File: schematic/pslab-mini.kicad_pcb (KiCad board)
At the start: 2 copper layers, 0 parts

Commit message: Adding PCB Floorplan
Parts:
- added C1: 22uF, Capacitor_SMD:C_0805_2012Metric, F.Cu at (233.7, 71.1)
- added C10: 100nF, Capacitor_SMD:C_0603_1608Metric, F.Cu at (189.8, 50.0)
- added C11: 10uF, Capacitor_SMD:C_0805_2012Metric, F.Cu at (238.2, 74.1)
- added C12: 22uF, Capacitor_SMD:C_0805_2012Metric, F.Cu at (238.2, 77.1)
- added C13: 22uF, Capacitor_SMD:C_0805_2012Metric, F.Cu at (238.2, 80.2)
- added C14: 5.6pF, Capacitor_SMD:C_0603_1608Metric, F.Cu at (189.8, 52.5)
- added C15: 100nF, Capacitor_SMD:C_0603_1608Metric, F.Cu at (189.8, 55.0)
- added C16: 5.6pF, Capacitor_SMD:C_0603_1608Metric, F.Cu at (189.8, 57.5)
- added C17: 100nF, Capacitor_SMD:C_0603_1608Metric, F.Cu at (189.8, 60.0)
- added C18: 1uF, Capacitor_SMD:C_0603_1608Metric, F.Cu at (189.8, 62.5)
- added C19: 100nF, Capacitor_SMD:C_0603_1608Metric, F.Cu at (189.8, 65.0)
- added C2: 22uF, Capacitor_SMD:C_0805_2012Metric, F.Cu at (233.7, 74.1)
- added C20: 10pF, Capacitor_SMD:C_0603_1608Metric, F.Cu at (189.8, 67.5)
- added C21: 100nF, Capacitor_SMD:C_0603_1608Metric, F.Cu at (189.8, 70.1)
- added C22: 10uF, Capacitor_SMD:C_0805_2012Metric, F.Cu at (238.2, 83.2)
- added C23: 100nF, Capacitor_SMD:C_0603_1608Metric, F.Cu at (189.8, 72.6)
- added C24: 10pF, Capacitor_SMD:C_0603_1608Metric, F.Cu at (193.8, 45.0)
- added C25: 100nF, Capacitor_SMD:C_0603_1608Metric, F.Cu at (193.8, 47.5)
- added C26: 2.2uF, Capacitor_SMD:C_0805_2012Metric, F.Cu at (238.2, 86.2)
- added C27: 22uF, Capacitor_SMD:C_0805_2012Metric, F.Cu at (242.6, 71.1)
- added C28: 4.7uF, Capacitor_SMD:C_0805_2012Metric, F.Cu at (242.6, 74.1)
- added C29: 2.2uF, Capacitor_SMD:C_0805_2012Metric, F.Cu at (242.6, 77.1)
- added C3: 2.2uF, Capacitor_SMD:C_0805_2012Metric, F.Cu at (233.7, 77.1)
- added C30: 100nF, Capacitor_SMD:C_0603_1608Metric, F.Cu at (193.8, 50.0)
- added C31: 1uF, Capacitor_SMD:C_0603_1608Metric, F.Cu at (193.8, 52.5)
- added C32: 100nF, Capacitor_SMD:C_0603_1608Metric, F.Cu at (193.8, 55.0)
- added C33: 10nF, Capacitor_SMD:C_0603_1608Metric, F.Cu at (193.8, 57.5)
- added C34: 1uF, Capacitor_SMD:C_0603_1608Metric, F.Cu at (193.8, 60.0)
- added C35: 10pF, Capacitor_SMD:C_0603_1608Metric, F.Cu at (193.8, 62.5)
- added C36: 10pF, Capacitor_SMD:C_0603_1608Metric, F.Cu at (193.8, 65.0)
- added C37: 10uF, Capacitor_SMD:C_0805_2012Metric, F.Cu at (242.6, 80.2)
- added C38: 1uF, Capacitor_SMD:C_0603_1608Metric, F.Cu at (193.8, 67.5)
- added C39: 0.1uF, Capacitor_SMD:C_0603_1608Metric, F.Cu at (193.8, 70.1)
- added C4: 1uF, Capacitor_SMD:C_0603_1608Metric, F.Cu at (189.8, 45.0)
- added C40: 0.1uF, Capacitor_SMD:C_0603_1608Metric, F.Cu at (193.8, 72.6)
- added C41: 1uF, Capacitor_SMD:C_0603_1608Metric, F.Cu at (197.9, 45.0)
- added C42: 10uF, Capacitor_SMD:C_0805_2012Metric, F.Cu at (242.6, 83.2)
- added C43: 1uF, Capacitor_SMD:C_0603_1608Metric, F.Cu at (197.9, 47.5)
- added C44: 1.2pF, Capacitor_SMD:C_0603_1608Metric, F.Cu at (197.9, 50.0)
- added C45: 1.2pF, Capacitor_SMD:C_0603_1608Metric, F.Cu at (197.9, 52.5)
- added C5: 22uF, Capacitor_SMD:C_0805_2012Metric, F.Cu at (233.7, 80.2)
- added C6: 12pF, Capacitor_SMD:C_0603_1608Metric, F.Cu at (189.8, 47.5)
- added C7: 10uF, Capacitor_SMD:C_0805_2012Metric, F.Cu at (233.7, 83.2)
- added C8: 22uF, Capacitor_SMD:C_0805_2012Metric, F.Cu at (233.7, 86.2)
- added C9: 22uF, Capacitor_SMD:C_0805_2012Metric, F.Cu at (238.2, 71.1)
- added D1: K1N5817HW-7-F, Diode_SMD:D_SOD-123, F.Cu at (182.6, 94.1)
- added D10: White, LED_SMD:LED_0603_1608Metric, F.Cu at (150.7, 105.7)
- added D11: GREEN, LED_SMD:LED_0805_2012Metric, F.Cu at (124.8, 70.8)
- added D12: BLUE, LED_SMD:LED_0805_2012Metric, F.Cu at (160.2, 106.0)
- added D2: 1N4148W, Diode_SMD:D_SOD-123, F.Cu at (182.6, 97.5)
- added D3: 6.8V, Diode_SMD:D_SOD-123, F.Cu at (182.6, 100.8)
- added D4: 6.8V, Diode_SMD:D_SOD-123, F.Cu at (182.6, 104.2)
- added D5: 1N4148W, Diode_SMD:D_SOD-123, F.Cu at (182.6, 107.5)
- added D6: WS2812B, LED_SMD:LED_WS2812B_PLCC4_5.0x5.0mm_P3.2mm, F.Cu at (198.8, 105.8)
- added D7: White, LED_SMD:LED_0603_1608Metric, F.Cu at (150.7, 97.9)
- added D8: White, LED_SMD:LED_0603_1608Metric, F.Cu at (150.7, 100.5)
- added D9: White, LED_SMD:LED_0603_1608Metric, F.Cu at (150.7, 103.1)
- added F1: 1A, Fuse:Fuse_1206_3216Metric, F.Cu at (152.2, 94.2)
- added FID1: Fiducial, Fiducial:Fiducial_0.5mm_Mask1.5mm, F.Cu at (87.5, 55.2)
- added FID2: Fiducial, Fiducial:Fiducial_0.5mm_Mask1.5mm, F.Cu at (81.2, 101.0)
- added FID3: Fiducial, Fiducial:Fiducial_0.5mm_Mask1.5mm, F.Cu at (153.5, 107.5)
- added FLASH1: W25Q32JV, Package_SO:SOIC-8_5.3x5.3mm_P1.27mm, F.Cu at (93.0, 78.8)
- added J1: USB_C_Receptacle_USB2.0_16P, Connector_USB:USB_C_Receptacle_G-Switch_GT-USB-7010ASV, F.Cu at (160.9, 99.0)
- added J2: Battery_Cell, pslab-mini:2.0mm_connector_edge, F.Cu at (90.8, 99.6)
- added J3: Conn_Coaxial, pslab-mini:BNC_connector_dosinconn DOSIN-801-0050, F.Cu at (157.0, 81.2)
- added J4: Conn_Coaxial, pslab-mini:BNC_connector_dosinconn DOSIN-801-0050, F.Cu at (157.0, 62.2)
- added J6: Conn_01x16_Socket, Connector_PinSocket_2.54mm:PinSocket_1x16_P2.54mm_Vertical, F.Cu at (97.5, 106.0)
- added J7: Conn_02x03_Top_Bottom, TerminalBlock_WAGO:TerminalBlock_WAGO_233-503_2x03_P2.54mm, F.Cu at (83.9, 88.2)
- added J8: Conn_02x17_Odd_Even, Connector_PinSocket_2.54mm:PinSocket_2x17_P2.54mm_Vertical, F.Cu at (91.5, 55.5)
- added L1: 3.3uH, Inductor_SMD:L_0603_1608Metric, F.Cu at (197.9, 55.0)
- added L2: 3.3uH, Inductor_SMD:L_0603_1608Metric, F.Cu at (197.9, 57.5)
- added L3: 4.7uH, Inductor_SMD:L_0805_2012Metric, F.Cu at (210.6, 110.6)
- added L4: 3.3uH, Inductor_SMD:L_0603_1608Metric, F.Cu at (197.9, 60.0)
- added L5: 2.4nH, Inductor_SMD:L_0402_1005Metric, F.Cu at (243.4, 66.7)
- added MH1: MountingHole_Pad, pslab-mini:MountingHole_2.75mm_Pad, F.Cu at (82.8, 56.8)
- added MH2: MountingHole_Pad, pslab-mini:MountingHole_2.75mm_Pad, F.Cu at (140.8, 56.8)
- added MH3: MountingHole_Pad, pslab-mini:MountingHole_2.75mm_Pad, F.Cu at (140.8, 105.8)
- added MH4: MountingHole_Pad, pslab-mini:MountingHole_2.75mm_Pad, F.Cu at (82.8, 105.8)
- added NT1: NetTie_2, NetTie:NetTie-2_SMD_Pad0.5mm, F.Cu at (243.1, 88.4)
- added NT2: NetTie_2, NetTie:NetTie-2_SMD_Pad0.5mm, F.Cu at (243.1, 89.9)
- added NT3: NetTie_2, NetTie:NetTie-2_SMD_Pad0.5mm, F.Cu at (243.1, 91.4)
- added NT4: NetTie_2, NetTie:NetTie-2_SMD_Pad0.5mm, F.Cu at (243.1, 92.9)
- added NT5: NetTie_2, NetTie:NetTie-2_SMD_Pad0.5mm, F.Cu at (243.1, 94.4)
- added PCB_ANT1: ANT, Diode_SMD:D_1206_3216Metric, F.Cu at (83.2, 72.5)
- added Q1: MMBT3904, Package_TO_SOT_SMD:SOT-23, F.Cu at (218.0, 102.2)
- added Q2: MMBT3906, Package_TO_SOT_SMD:SOT-23, F.Cu at (218.0, 106.8)
- added R1: 200k, Resistor_SMD:R_0603_1608Metric, F.Cu at (197.9, 62.5)
- added R10: 1k, Resistor_SMD:R_0603_1608Metric, F.Cu at (201.9, 55.0)
- added R11: 1k, Resistor_SMD:R_0603_1608Metric, F.Cu at (201.9, 57.5)
- added R12: 200, Resistor_SMD:R_0603_1608Metric, F.Cu at (201.9, 60.0)
- added R13: 200, Resistor_SMD:R_0603_1608Metric, F.Cu at (201.9, 62.5)
- added R14: 200, Resistor_SMD:R_0603_1608Metric, F.Cu at (201.9, 65.0)
- added R16: 5k1, Resistor_SMD:R_0603_1608Metric, F.Cu at (201.9, 70.1)
- added R17: 10k, Resistor_SMD:R_0603_1608Metric, F.Cu at (201.9, 72.6)
- added R18: 200, Resistor_SMD:R_0603_1608Metric, F.Cu at (205.9, 45.0)
- added R19: 200, Resistor_SMD:R_0603_1608Metric, F.Cu at (205.9, 47.5)
- added R2: 200k, Resistor_SMD:R_0603_1608Metric, F.Cu at (197.9, 65.0)
- added R20: 5k1, Resistor_SMD:R_0603_1608Metric, F.Cu at (205.9, 50.0)
- added R21: 5k1, Resistor_SMD:R_0603_1608Metric, F.Cu at (205.9, 52.5)
- added R22: 200, Resistor_SMD:R_0603_1608Metric, F.Cu at (205.9, 55.0)
- added R23: 200, Resistor_SMD:R_0603_1608Metric, F.Cu at (205.9, 57.5)
- added R24: 5k1, Resistor_SMD:R_0603_1608Metric, F.Cu at (205.9, 60.0)
- added R25: 5k1, Resistor_SMD:R_0603_1608Metric, F.Cu at (205.9, 62.5)
- added R26: 10k, Resistor_SMD:R_0603_1608Metric, F.Cu at (205.9, 65.0)
- added R27: 10k, Resistor_SMD:R_0603_1608Metric, F.Cu at (205.9, 67.5)
- added R28: 10k, Resistor_SMD:R_0603_1608Metric, F.Cu at (205.9, 70.1)
- added R29: 10k, Resistor_SMD:R_0603_1608Metric, F.Cu at (205.9, 72.6)
- added R3: 51k, Resistor_SMD:R_0603_1608Metric, F.Cu at (197.9, 67.5)
- added R30: 10k, Resistor_SMD:R_0603_1608Metric, F.Cu at (209.9, 45.0)
- added R31: 200k, Resistor_SMD:R_0603_1608Metric, F.Cu at (209.9, 47.5)
- added R32: 10k, Resistor_SMD:R_0603_1608Metric, F.Cu at (209.9, 50.0)
- added R33: 1M, Resistor_SMD:R_0603_1608Metric, F.Cu at (209.9, 52.5)
- added R34: 200k, Resistor_SMD:R_0603_1608Metric, F.Cu at (209.9, 55.0)
- added R35: 1M, Resistor_SMD:R_0603_1608Metric, F.Cu at (209.9, 57.5)
- added R36: 0, Resistor_SMD:R_0603_1608Metric, F.Cu at (209.9, 60.0)
- added R37: 10k, Resistor_SMD:R_0603_1608Metric, F.Cu at (209.9, 62.5)
- added R38: 0, Resistor_SMD:R_0603_1608Metric, F.Cu at (209.9, 65.0)
- added R39: 0, Resistor_SMD:R_0603_1608Metric, F.Cu at (209.9, 67.5)
- added R4: 5k1, Resistor_SMD:R_0603_1608Metric, F.Cu at (197.9, 70.1)
- added R40: 0, Resistor_SMD:R_0603_1608Metric, F.Cu at (209.9, 70.1)
- added R5: 5k1, Resistor_SMD:R_0603_1608Metric, F.Cu at (197.9, 72.6)
- added R6: 100k, Resistor_SMD:R_0603_1608Metric, F.Cu at (201.9, 45.0)
- added R7: 10k, Resistor_SMD:R_0603_1608Metric, F.Cu at (201.9, 47.5)
- added R8: 180k, Resistor_SMD:R_0603_1608Metric, F.Cu at (201.9, 50.0)
- added R9: 30k, Resistor_SMD:R_0603_1608Metric, F.Cu at (201.9, 52.5)
- added SW1: Power, Button_Switch_SMD:SW_Tactile_SPST_NO_Straight_CK_PTS636Sx25SMTRLFS, F.Cu at (193.8, 81.3)
- added SW2: Reset, Button_Switch_SMD:SW_Tactile_SPST_NO_Straight_CK_PTS636Sx25SMTRLFS, F.Cu at (193.8, 88.3)
- added TP1: TestPoint, pslab-mini:Test_Point_0.8mm, F.Cu at (245.2, 47.7)
- added TP2: TestPoint, pslab-mini:Test_Point_0.8mm, F.Cu at (245.2, 49.9)
- added TP3: TestPoint, pslab-mini:Test_Point_0.8mm, F.Cu at (245.2, 52.1)
- added TP4: TestPoint, pslab-mini:Test_Point_0.8mm, F.Cu at (245.2, 54.3)
- added TP5: TestPoint, pslab-mini:Test_Point_0.8mm, F.Cu at (245.2, 56.5)
- added TP6: D+, TestPoint:TestPoint_Pad_1.0x1.0mm, F.Cu at (205.3, 91.0)
- added TP7: D-, TestPoint:TestPoint_Pad_1.0x1.0mm, F.Cu at (205.2, 77.8)
- added TP8: VINBUS, TestPoint:TestPoint_Pad_1.0x1.0mm, F.Cu at (205.2, 82.0)
- added TP9: GND, TestPoint:TestPoint_Pad_1.0x1.0mm, F.Cu at (205.2, 86.5)
- added U1: MT1470, Package_TO_SOT_SMD:SOT-23-6, F.Cu at (213.1, 85.0)
- added U10: TL082, Package_SO:SOIC-8_3.9x4.9mm_P1.27mm, F.Cu at (227.3, 92.7)
- added U11: ESP32-C3, Package_DFN_QFN:QFN-32-1EP_5x5mm_P0.5mm_EP3.7x3.7mm, F.Cu at (92.8, 70.2)
- added U2: AP3015A, Package_TO_SOT_SMD:SOT-23-5, F.Cu at (212.6, 92.2)
- added U3: IP5189T, Package_DFN_QFN:QFN-24-1EP_4x4mm_P0.5mm_EP2.6x2.6mm, F.Cu at (145.8, 97.2)
- added U4: SP0503BAHT, Package_TO_SOT_SMD:SOT-143, F.Cu at (244.1, 63.5)
- added U5: AMS1117-3.3, Package_TO_SOT_SMD:SOT-223-3_TabPin2, F.Cu at (237.0, 65.2)
- added U6: STM32H563RIT6, Package_QFP:LQFP-64_10x10mm_P0.5mm, F.Cu at (112.5, 88.0)
- added U7: TL082, Package_SO:SOIC-8_3.9x4.9mm_P1.27mm, F.Cu at (227.3, 73.0)
- added U8: MCP6S21, Package_SO:SOIC-8_3.9x4.9mm_P1.27mm, F.Cu at (227.3, 79.6)
- added U9: MCP6S21, Package_SO:SOIC-8_3.9x4.9mm_P1.27mm, F.Cu at (227.3, 86.1)
- added X1: 32kHz768, Crystal:Crystal_SMD_3215-2Pin_3.2x1.5mm, F.Cu at (115.8, 72.5)
- added Y1: Crystal_25MHz, Crystal:Crystal_SMD_5032-4Pin_5.0x3.2mm, F.Cu at (110.0, 74.2)
- added Y2: Crystal_40Mhz, Crystal:Crystal_SMD_3225-4Pin_3.2x2.5mm, F.Cu at (99.5, 70.0)
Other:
- board outline added: 85 x 56 mm
- copper layers 2 -> 4

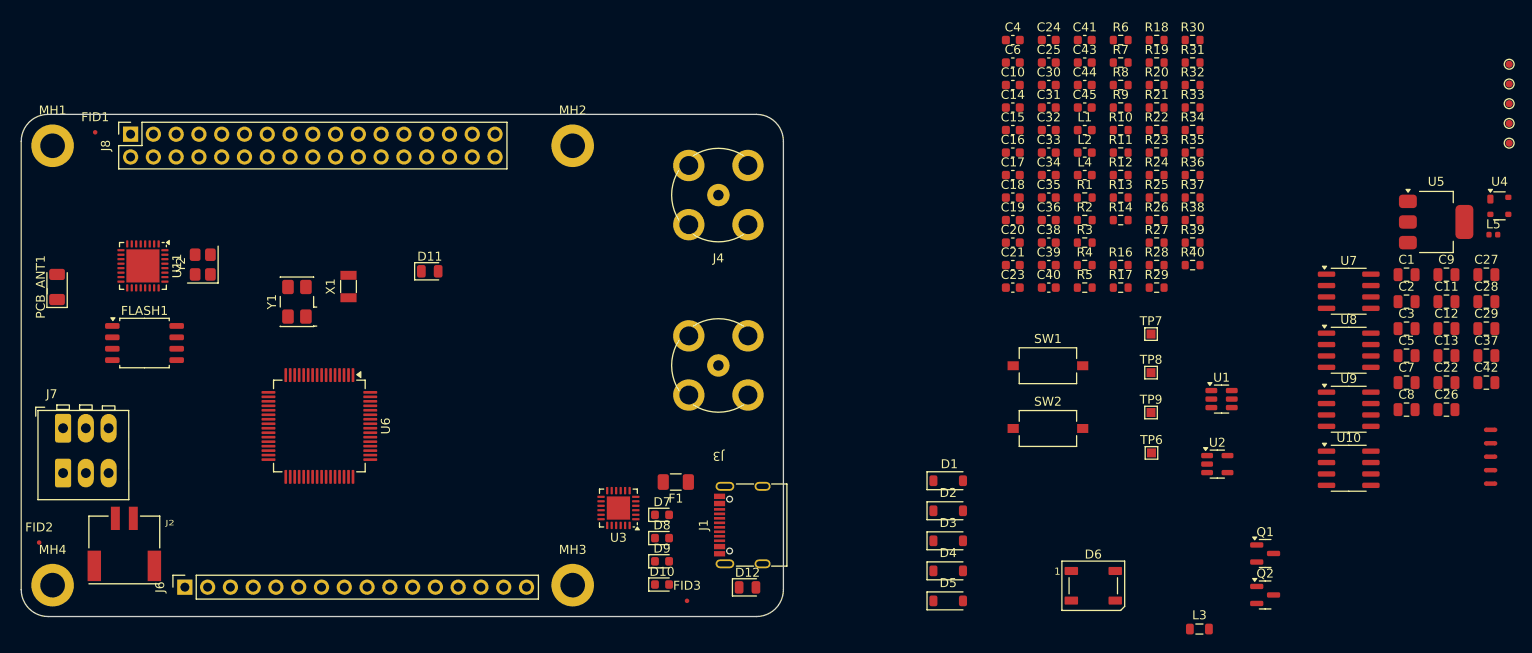
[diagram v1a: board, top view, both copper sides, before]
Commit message: Adding major components to the layout
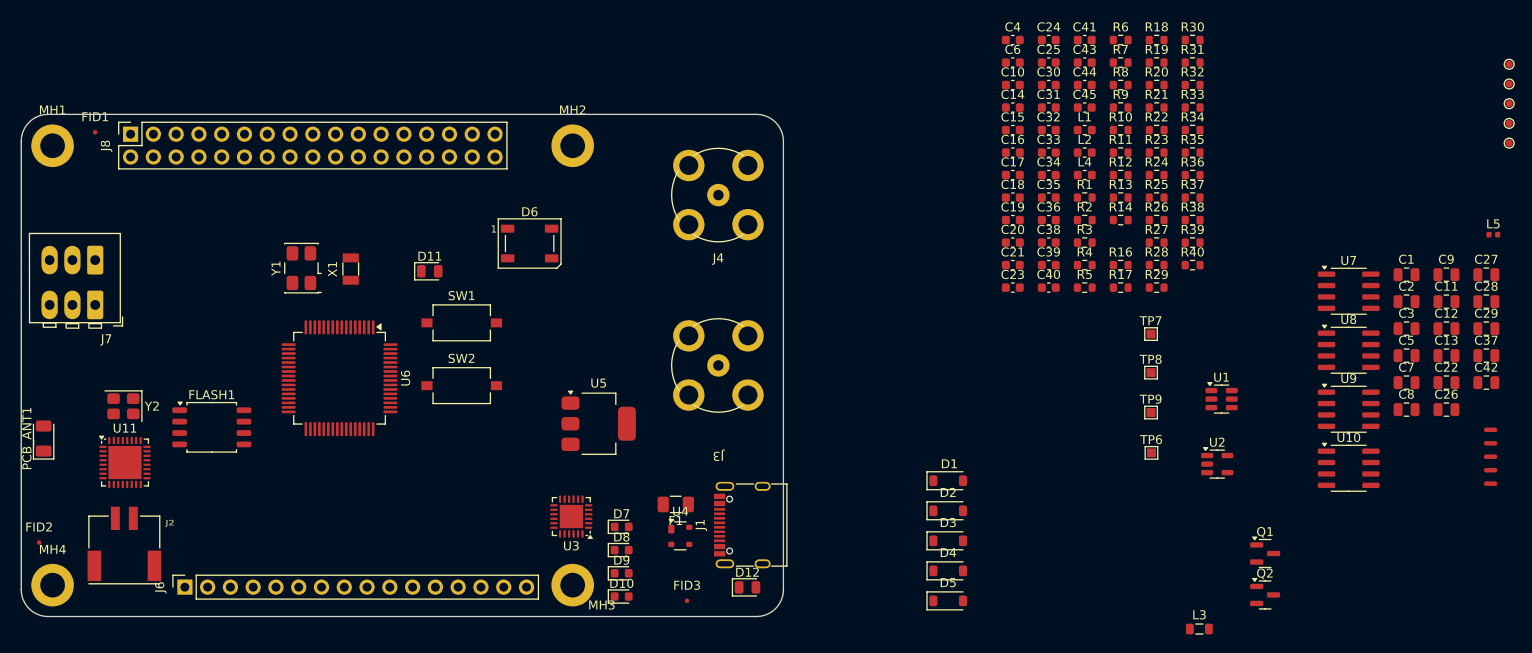
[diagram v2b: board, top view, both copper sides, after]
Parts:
- moved U4 98.5 mm to (152.8, 100.2)
- moved U5 96.1 mm to (143.7, 87.8)
- moved D6 73.5 mm to (135.9, 67.7)
- moved SW1 65.5 mm to (128.4, 76.5)
- moved SW2 65.5 mm to (128.4, 83.5)
- moved U11 22.0 mm to (90.8, 92.1), turned to 0 degrees
- moved Y2 18.1 mm to (90.7, 85.8), turned to 180 degrees
- moved PCB_ANT1 17.0 mm to (81.8, 89.4)
- moved J7 14.2 mm to (87.5, 74.5), turned to 180 degrees
- moved FLASH1 12.0 mm to (100.5, 88.2)
- moved U6 5.78 mm to (114.8, 82.7)
- moved U3 5.34 mm to (140.6, 98.1)
- moved D7 4.70 mm to (146.2, 99.2)
- moved D8 4.70 mm to (146.2, 101.8)
- moved D9 4.70 mm to (146.2, 104.4)
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
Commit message: Completed layout
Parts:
- D+: renamed from TP7; moved to B.Cu
- D-: renamed from TP8; moved to B.Cu
- GND: renamed from TP9; moved to B.Cu
- J7: footprint TerminalBlock_WAGO:TerminalBlock_WAGO_233-503_2x03_P2.54mm -> pslab-mini:pslab-mini_2x03_P2.54mm
- VUSBIN: renamed from TP6; moved to B.Cu
- moved L5 156.9 mm to (88.3, 90.5)
- moved C42 151.8 mm to (91.2, 94.7), turned to 90 degrees
- moved C37 148.8 mm to (94.2, 89.3), turned to 180 degrees
- moved U9 133.6 mm to (93.8, 83.2), turned to 90 degrees
- moved U10 133.1 mm to (96.5, 68.1)
- moved C26 131.3 mm to (108.8, 63.8), turned to 180 degrees
- moved C29 128.4 mm to (114.4, 84.0)
- moved C28 128.1 mm to (115.0, 63.5)
- moved U8 127.3 mm to (100.0, 79.8), turned to 90 degrees
- moved R37 125.6 mm to (89.0, 96.6), turned to 90 degrees
- moved R32 123.9 mm to (89.8, 80.2), turned to -90 degrees
- moved R30 122.0 mm to (92.4, 78.0), turned to 180 degrees
- moved C43 121.2 mm to (87.1, 96.7), turned to 90 degrees
- moved TP1 121.1 mm to (130.1, 85.3)
- moved R35 119.5 mm to (90.5, 62.5), turned to 90 degrees
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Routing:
- net Net-(NT4-Pad1): track 0.00 -> 1.22 mm
- net Net-(NT3-Pad1): track 0.00 -> 1.15 mm
- net Net-(NT2-Pad1): track 0.00 -> 1.00 mm
- net Net-(NT5-Pad1): track 0.00 -> 1.00 mm
- net Net-(NT1-Pad1): track 0.00 -> 0.96 mm
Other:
- board text added: "+6V"
- board text added: "+9V"
- board text added: "-6V"
- board text added: "-9V"
- board text added: "VDDA"

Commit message: pcb
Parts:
- moved R12 1.27 mm to (110.5, 61.5), turned to 0 degrees
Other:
- board text added: "Analog"
- board text added: "Digital"
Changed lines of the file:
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@@
 		(tags "capacitor")
 		(property "Reference" "C28"
-			(at 0 -1.68 0)
+			(at -2.45 0.5 0)
 			(layer "F.SilkS")
 			(effects
@@
 	(footprint "Resistor_SMD:R_0603_1608Metric"
 		(layer "F.Cu")
-		(at 111.75 61.75 -90)
+		(at 110.5 61.5)
 		(descr "Resistor SMD 0603 (1608 Metric), square (rectangular) end terminal, IPC-7351 nominal, (Body size source: IPC-SM-782 page 72, https://www.pcb-3d.com/wordpress/wp-content/uploads/ipc-sm-782a_amendment_1_and_2.pdf), generated with kicad-footprint-generator")
 		(tags "resistor")
 		(property "Reference" "R12"
-			(at 0 -1.43 90)
+			(at 1.25 1.25 0)
 			(layer "F.SilkS")
 			(effects
@@
 		)
 		(property "Value" "200"
-			(at 0 1.43 90)
+			(at 0 1.43 0)
 			(layer "F.Fab")
 			(effects
@@
 		)
 		(property "Datasheet" "https://lcsc.com/datasheet/lcsc_datasheet_2506161100_YAGEO-RC0603FR-07200RL_C114664.pdf"
-			(at 0 0 90)
+			(at 0 0 0)
 			(layer "F.Fab")
 			(hide yes)
@@
 		)
 		(property "Description" "1/16W 5%"
-			(at 0 0 90)
+			(at 0 0 0)
 			(layer "F.Fab")
 			(hide yes)
@@
 		)
 		(property "Price" "0.1"
-			(at 0 0 270)
+			(at 0 0 0)
 			(unlocked yes)
 			(layer "F.Fab")
@@
 		)
 		(property "Mfr Number" "RC0603FR-07200RL"
-			(at 0 0 270)
+			(at 0 0 0)
 			(unlocked yes)
 			(layer "F.Fab")
@@
 		)
 		(property "Part Number (LCSC)" "C114664"
-			(at 0 0 270)
+			(at 0 0 0)
 			(unlocked yes)
 			(layer "F.Fab")
@@
 		(attr smd)
 		(fp_line
-			(start -0.237258 0.5225)
-			(end 0.237258 0.5225)
+			(start -0.237258 -0.5225)
+			(end 0.237258 -0.5225)
 			(stroke
 				(width 0.12)
@@
 		)
 		(fp_line
-			(start -0.237258 -0.5225)
-			(end 0.237258 -0.5225)
+			(start -0.237258 0.5225)
+			(end 0.237258 0.5225)
 			(stroke
 				(width 0.12)
@@
 		)
 		(fp_line
-			(start -1.48 0.73)
-			(end -1.48 -0.73)
+			(start -1.48 -0.73)
+			(end 1.48 -0.73)
 			(stroke
 				(width 0.05)
@@
 		)
 		(fp_line
-			(start 1.48 0.73)
-			(end -1.48 0.73)
+			(start -1.48 0.73)
+			(end -1.48 -0.73)
 			(stroke
 				(width 0.05)
@@
 		)
 		(fp_line
-			(start -1.48 -0.73)
-			(end 1.48 -0.73)
+			(start 1.48 -0.73)
+			(end 1.48 0.73)
 			(stroke
 				(width 0.05)
@@
 		)
 		(fp_line
-			(start 1.48 -0.73)
-			(end 1.48 0.73)
+			(start 1.48 0.73)
+			(end -1.48 0.73)
 			(stroke
 				(width 0.05)
@@
 		)
 		(fp_line
-			(start -0.8 0.4125)
-			(end -0.8 -0.4125)
+			(start -0.8 -0.4125)
+			(end 0.8 -0.4125)
 			(stroke
 				(width 0.1)
@@
 		)
 		(fp_line
-			(start 0.8 0.4125)
-			(end -0.8 0.4125)
+			(start -0.8 0.4125)
+			(end -0.8 -0.4125)
 			(stroke
 				(width 0.1)
@@
 		)
 		(fp_line
-			(start -0.8 -0.4125)
-			(end 0.8 -0.4125)
+			(start 0.8 -0.4125)
+			(end 0.8 0.4125)
 			(stroke
 				(width 0.1)
@@
 		)
 		(fp_line
-			(start 0.8 -0.4125)
-			(end 0.8 0.4125)
+			(start 0.8 0.4125)
+			(end -0.8 0.4125)
 			(stroke
 				(width 0.1)
@@
 		)
 		(fp_text user "${REFERENCE}"
-			(at 0 0 90)
+			(at 0 0 0)
 			(layer "F.Fab")
 			(effects
@@
 		)
 		(pad "1" smd roundrect
-			(at -0.825 0 270)
+			(at -0.825 0)
 			(size 0.8 0.95)
 			(layers "F.Cu" "F.Mask" "F.Paste")
@@
 		)
 		(pad "2" smd roundrect
-			(at 0.825 0 270)
+			(at 0.825 0)
 			(size 0.8 0.95)
 			(layers "F.Cu" "F.Mask" "F.Paste")
@@
 	)
 	(gr_line
+		(start 121 60)
+		(end 131 60)
+		(stroke
+			(width 0.1)
+			(type default)
+		)
+		(layer "F.SilkS")
+	)
+	(gr_line
+		(start 135.325 57.4875)
+		(end 135.1 57.7125)
+		(stroke
+			(width 0.1)
+			(type default)
+		)
+		(layer "F.SilkS")
+	)
+	(gr_line
+		(start 135.075 57.2375)
+		(end 135.325 57.4875)
+		(stroke
+			(width 0.1)
+			(type default)
+		)
+		(layer "F.SilkS")
+	)
+	(gr_line
+		(start 134.575 59.5125)
+		(end 134.35 59.2875)
+		(stroke
+			(width 0.1)
+			(type default)
+		)
+		(layer "F.SilkS")
+	)
+	(gr_line
+		(start 135.325 57.4875)
+		(end 134.575 57.4875)
+		(stroke
+			(width 0.1)
+			(type default)
+		)
+		(layer "F.SilkS")
+	)
+	(gr_line
+		(start 121 59.5)
+		(end 121 60)
+		(stroke
+			(width 0.1)
+			(type default)
+		)
+		(layer "F.SilkS")
+	)
+	(gr_line
+		(start 134.8 59.2875)
+		(end 134.575 59.5125)
+		(stroke
+			(width 0.1)
+			(type default)
+		)
+		(layer "F.SilkS")
+	)
+	(gr_line
+		(start 131 60)
+		(end 131 59.5)
+		(stroke
+			(width 0.1)
+			(type default)
+		)
+		(layer "F.SilkS")
+	)
+	(gr_line
+		(start 110.75 59.5)
+		(end 110.75 60)
+		(stroke
+			(width 0.1)
+			(type default)
+		)
+		(layer "F.SilkS")
+	)
+	(gr_line
+		(start 134.9 57.4875)
+		(end 134.9 58.2375)
+		(stroke
+			(width 0.1)
+			(type default)
+		)
+		(layer "F.SilkS")
+	)
+	(gr_line
+		(start 134.575 59.5125)
+		(end 134.8 59.2875)
+		(stroke
+			(width 0.1)
+			(type default)
+		)
+		(layer "F.SilkS")
+	)
+	(gr_line
+		(start 120.5 60)
+		(end 120.5 59.5)
+		(stroke
+			(width 0.1)
+			(type default)
+		)
+		(layer "F.SilkS")
+	)
+	(gr_line
+		(start 134.15 58.2375)
+		(end 134.15 58.9875)
+		(stroke
+			(width 0.1)
+			(type default)
+		)
+		(layer "F.SilkS")
+	)
+	(gr_line
+		(start 134.575 57.4875)
+		(end 134.575 59.5125)
+		(stroke
+			(width 0.1)
+			(type default)
+		)
+		(layer "F.SilkS")
+	)
+	(gr_line
+		(start 135.325 57.4875)
+		(end 135.075 57.2375)
+		(stroke
+			(width 0.1)
+			(type default)
+		)
+		(layer "F.SilkS")
+	)
+	(gr_line
+		(start 134.9 58.2375)
+		(end 134.15 58.2375)
+		(stroke
+			(width 0.1)
+			(type default)
+		)
+		(layer "F.SilkS")
+	)
+	(gr_line
+		(start 134.15 58.9875)
+		(end 134.9 58.9875)
+		(stroke
+			(width 0.1)
+			(type default)
+		)
+		(layer "F.SilkS")
+	)
+	(gr_line
+		(start 134.15 57.4875)
+		(end 134.9 57.4875)
+		(stroke
+			(width 0.1)
+			(type default)
+		)
+		(layer "F.SilkS")
+	)
+	(gr_line
+		(start 110.75 60)
+		(end 120.5 60)
+		(stroke
+			(width 0.1)
+			(type default)
+		)
+		(layer "F.SilkS")
+	)
+	(gr_line
 		(start 82.25 109.25)
 		(end 161.25 109.25)
@@
 		(layer "Edge.Cuts")
 	)
+	(gr_text "Analog"
+		(at 114.5 60.75 0)
+		(layer "F.SilkS")
+		(effects
+			(font
+				(size 0.5 0.5)
+				(thickness 0.1)
+				(bold yes)
+			)
+			(justify left bottom)
+		)
+	)
+	(gr_text "Digital"
+		(at 124.75 60.75 0)
+		(layer "F.SilkS")
+		(effects
+			(font
+				(size 0.5 0.5)
+				(thickness 0.1)
+				(bold yes)
+			)
+			(justify left bottom)
+		)
+	)
 	(gr_text "-6V"

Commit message: new layout
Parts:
- removed R12, R13: 200, Resistor_SMD:R_0603_1608Metric
- removed the R14 at (102.2, 61.5)
- added R24: 200, Resistor_SMD:R_0603_1608Metric, F.Cu at (109.2, 49.8)
- added R40: 200, Resistor_SMD:R_0603_1608Metric, F.Cu at (114.2, 50.0)
- added R41: 200, Resistor_SMD:R_0603_1608Metric, F.Cu at (118.3, 50.1)
- D+1: renamed from D+; value D- -> TP7
- D-1: renamed from D-; value VINBUS -> TP8
- GND1: renamed from GND; value GND -> TP9
- VUSBIN1: renamed from VUSBIN; value D+ -> TP6
- moved R34 38.9 mm to (129.3, 64.9), turned to 0 degrees
- moved R33 35.8 mm to (127.0, 67.1), turned to 180 degrees
- moved R32 33.5 mm to (129.2, 61.3), turned to 180 degrees
- moved R31 30.9 mm to (117.7, 67.0), turned to 180 degrees
- moved U10 27.3 mm to (123.4, 63.3), turned to 180 degrees
- moved R28 24.0 mm to (117.6, 65.1), turned to 180 degrees
- moved U9 20.3 mm to (104.8, 66.2), turned to -90 degrees
- moved FLASH1 20.1 mm to (96.8, 79.2), turned to 0 degrees
- moved R30 16.6 mm to (117.6, 63.2), turned to 0 degrees
- moved C28 16.4 mm to (102.8, 74.5), turned to 180 degrees
- moved R25 16.1 mm to (110.7, 63.5), turned to 0 degrees
- moved R29 15.1 mm to (99.9, 64.9), turned to 90 degrees
- moved U8 15.0 mm to (110.9, 69.5), turned to -90 degrees
- moved R14 11.8 mm to (104.9, 49.8)
- moved C23 10.9 mm to (105.0, 76.6), turned to 180 degrees
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- renumbered J8 to J5, R16 to R14, R17 to R15, R18 to R16, R19 to R17, R20 to R18, R21 to R19, R22 to R20, R23 to R21, R24 to R22, R25 to R23, R26 to R25, R27 to R26, R28 to R27, R29 to R28, R30 to R29, R31 to R30, R32 to R31, R33 to R32, R34 to R33, R35 to R34, R36 to R35, R37 to R36, R38 to R37, R39 to R38, R40 to R39, SW2 to SW1, SW1 to SW2
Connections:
- J5 pad 10: /VOL -> /GPIO4
- J5 pad 12: /RES -> /GPIO3
- J5 pad 14: /CAP -> /GPIO2
- J5 pad 16: /FQY -> /GPIO1
- J5 pad 2: /CH1 -> /SQR
- J5 pad 20: /GPIO1 -> /FQY
- J5 pad 22: /GPIO2 -> /CAP
- J5 pad 24: /GPIO3 -> /RES
- J5 pad 26: /GPIO4 -> /VOL
- J5 pad 28: /GPIO5 -> /LA2
- J5 pad 30: /GPIO6 -> /LA1
- J5 pad 32: /GPIO7 -> /CH2
- J5 pad 34: /SQR -> /CH1
- J5 pad 4: /CH2 -> /GPIO7
- J5 pad 6: /LA1 -> /GPIO6
- J5 pad 8: /LA2 -> /GPIO5
- J6 pad 3: /UART2_TX -> /UART6_TX
- J6 pad 4: /UART2_RX -> /UART6_RX
- R37 pad 1: /SPI1_SCK -> /SPI2_SCK
- R38 pad 1: /SPI1_MOSI -> /SPI2_MOSI
- R39 pad 1: /SPI1_MISO -> /SPI2_MISO
- U6 pad 16: /UART2_TX -> /CS1
- U6 pad 17: /UART2_RX -> /CS2
- U6 pad 2: /RGB -> /GPIO4
- U6 pad 22: /SPI1_MISO -> Net-(U6-PA6)
- U6 pad 27: /CS1 -> Net-(U6-PB1)
- U6 pad 28: /CS2 -> Net-(U6-PB2)
- U6 pad 35: Net-(U6-PB14) -> /SPI2_MISO
- U6 pad 37: Net-(U6-PC6) -> /UART6_TX
- U6 pad 38: Net-(U6-PC7) -> /UART6_RX
- U6 pad 61: /GPIO4 -> /RGB
- U8 pad 6: /SPI2_MOSI -> /SPI1_MOSI
- U8 pad 7: /SPI2_SCK -> /SPI1_SCK
- U9 pad 6: /SPI2_MOSI -> /SPI1_MOSI
- U9 pad 7: /SPI2_SCK -> /SPI1_SCK

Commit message: new routing
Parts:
- moved R39 21.0 mm to (90.9, 77.1), turned to -90 degrees
- moved R37 17.3 mm to (103.0, 79.8), turned to -90 degrees
- moved R38 12.8 mm to (100.6, 83.0)
- moved R25 3.23 mm to (113.9, 63.6)
- moved R32 2.86 mm to (132.1, 61.1)
- moved C33 1.95 mm to (119.2, 68.9)
- moved R27 1.69 mm to (119.1, 70.7)
- moved R33 1.61 mm to (127.2, 68.7)
- moved U7 1.41 mm to (124.6, 72.7)
- moved R26 1.30 mm to (123.5, 77.5)
- moved U10 1.30 mm to (123.4, 64.6)
- moved F1 1.18 mm to (147.7, 104.0)
- moved U8 0.63 mm to (110.9, 70.1)
- moved R1 0.62 mm to (138.8, 91.6)
- moved D10 0.23 mm to (146.2, 100.5)
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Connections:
- J5 pad 28: /LA2 -> /LA1
- J5 pad 30: /LA1 -> /LA2
- J5 pad 32: /CH2 -> /CH1
- J5 pad 34: /CH1 -> /CH2
- R24 pad 1: /LA2 -> /LA1
- R41 pad 1: /LA1 -> /LA2
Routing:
- net GND: track 0.00 -> 48.5 mm, vias 0 -> 15
- net /CH1: track 0.00 -> 42.6 mm
- net +3V3: track 0.00 -> 37.6 mm
- net /CH2: track 0.00 -> 29.1 mm
- net /CH1_IN: track 0.00 -> 25.8 mm
- net /VINPUT: track 0.00 -> 25.1 mm
- net /BAT+: track 0.00 -> 23.8 mm
- net /I2C1_SDA: track 0.00 -> 23.4 mm, vias 0 -> 2
- net /I2C1_SCL: track 0.00 -> 23.3 mm, vias 0 -> 2
- net VDDA: track 0.00 -> 22.2 mm
- net Net-(U9-CHA): track 0.00 -> 21.8 mm
- net /ESP_DATA_READY: track 0.00 -> 21.4 mm, vias 0 -> 2
- net /SPI3_SCK: track 0.00 -> 18.6 mm
- net /SPI.CS: track 0.00 -> 17.8 mm
- net /SPI3_MISO: track 0.00 -> 17.7 mm
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- added copper zone on In1.Cu, net GND
